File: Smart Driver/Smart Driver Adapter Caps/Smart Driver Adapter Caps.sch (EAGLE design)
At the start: 9 parts, among them U2 DRV8353HMRTATWQFN_HMRTAT_TEX-M

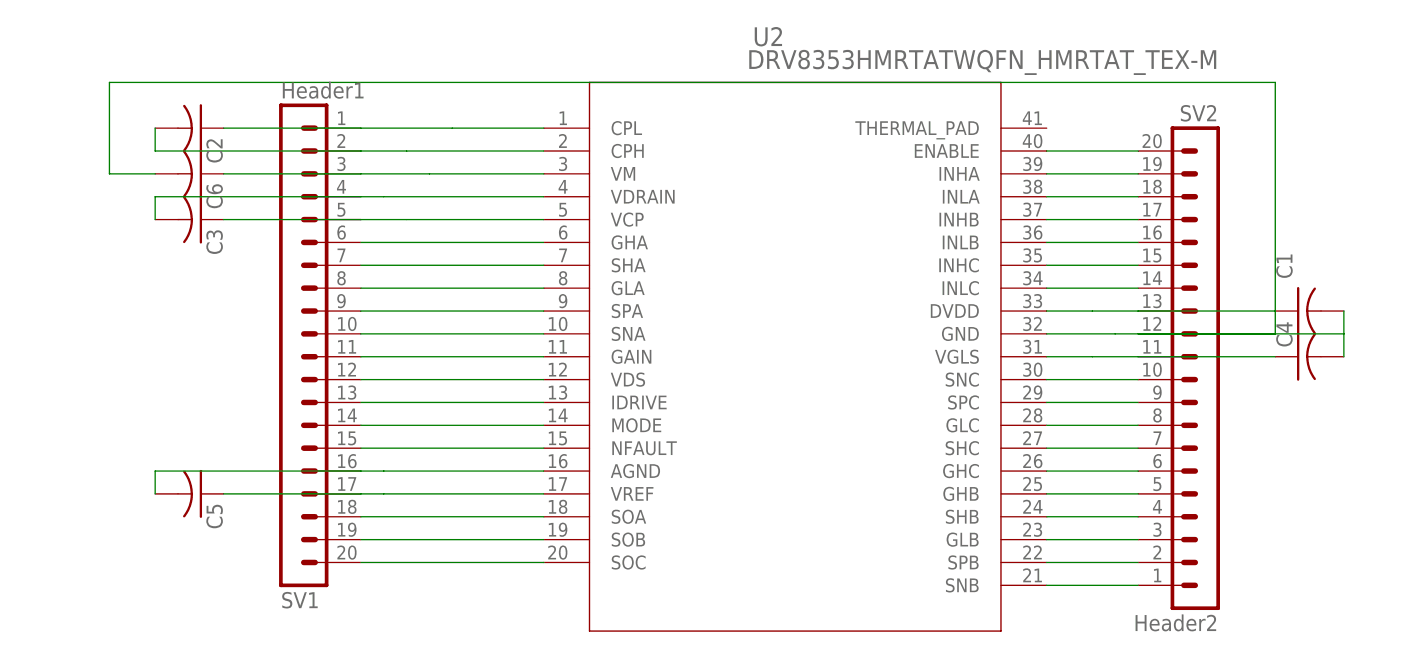
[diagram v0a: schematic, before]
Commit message: Corrected Adapter with Caps PCB
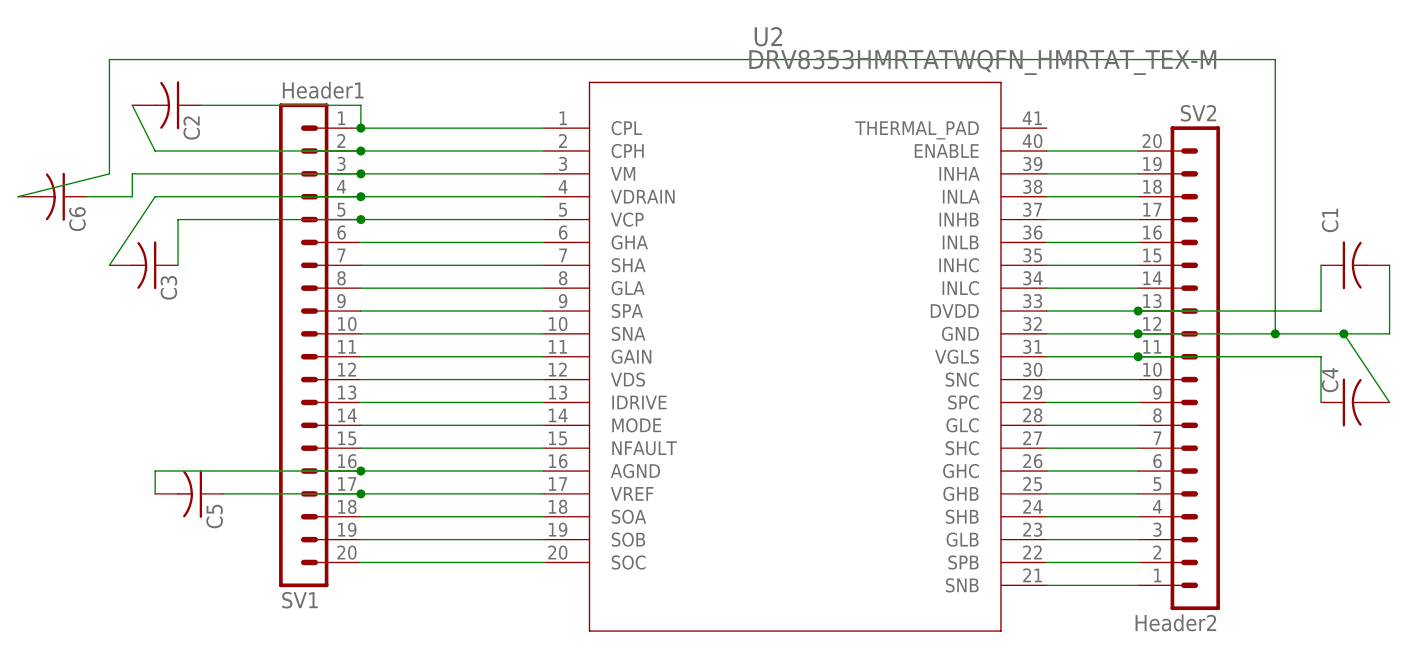
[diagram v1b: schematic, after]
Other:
- moved on the sheet: C1, C2, C3, C4, C6
